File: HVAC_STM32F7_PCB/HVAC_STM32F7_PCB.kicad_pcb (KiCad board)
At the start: 4 copper layers, 200 x 130 mm, 106 parts, among them J1 DC_Jack_5.5x2.1mm, J10 OUT_Signal_connector, J11 OUT_Signal_connector, J12 OUT_Signal_connector, J13 OUT_Signal_connector, J14 Signal_connector, J15 Signal_connector, J16 Signal_connector, J17 Signal_connector, J18 Conn_02x08_Odd_Even, J2 Signal_connector, J3 Signal_connector, J4 Signal_connector, J5 Signal_connector, J6 OUT_Signal_connector, J7 OUT_Signal_connector, J8 OUT_Signal_connector, J9 OUT_Signal_connector, Q1 AO4407A, SW1 ON/OFF, U1 LM2596S-5, U2 LM2596S-3.3, U3 DAC7568IAPW, U5 TLV9304xPW, U6 TLV9304xPW, U7 ADS8688

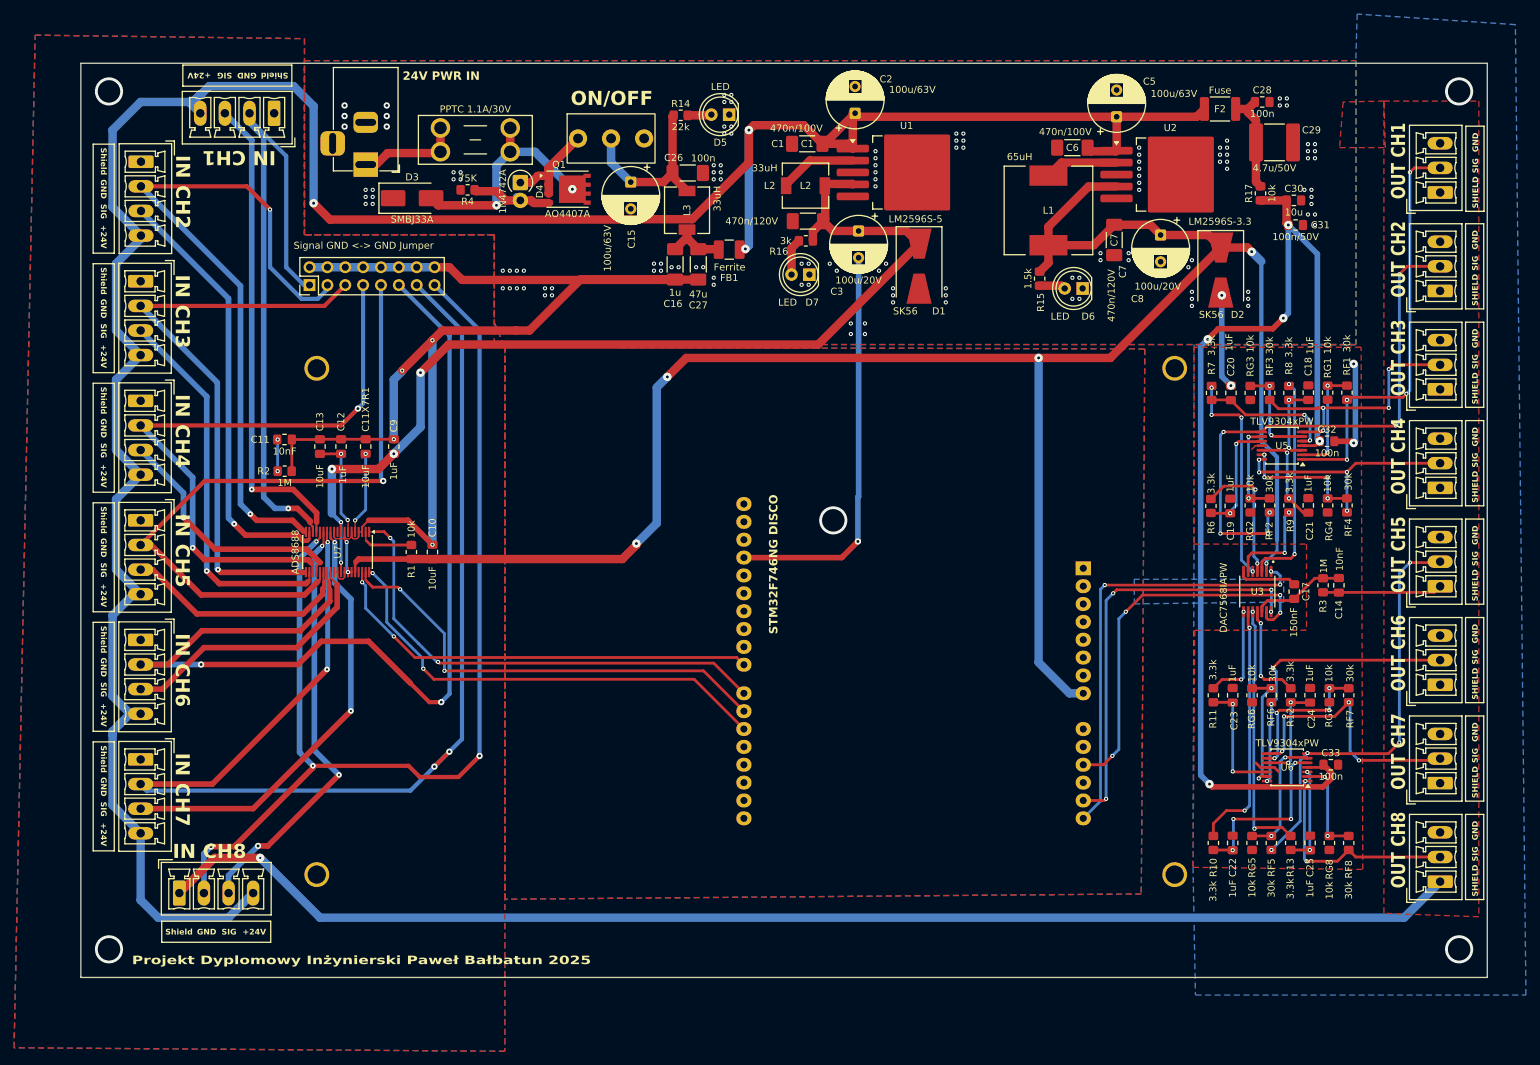
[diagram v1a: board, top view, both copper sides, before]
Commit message: ADD: poprawki pcb, nowe gerbery
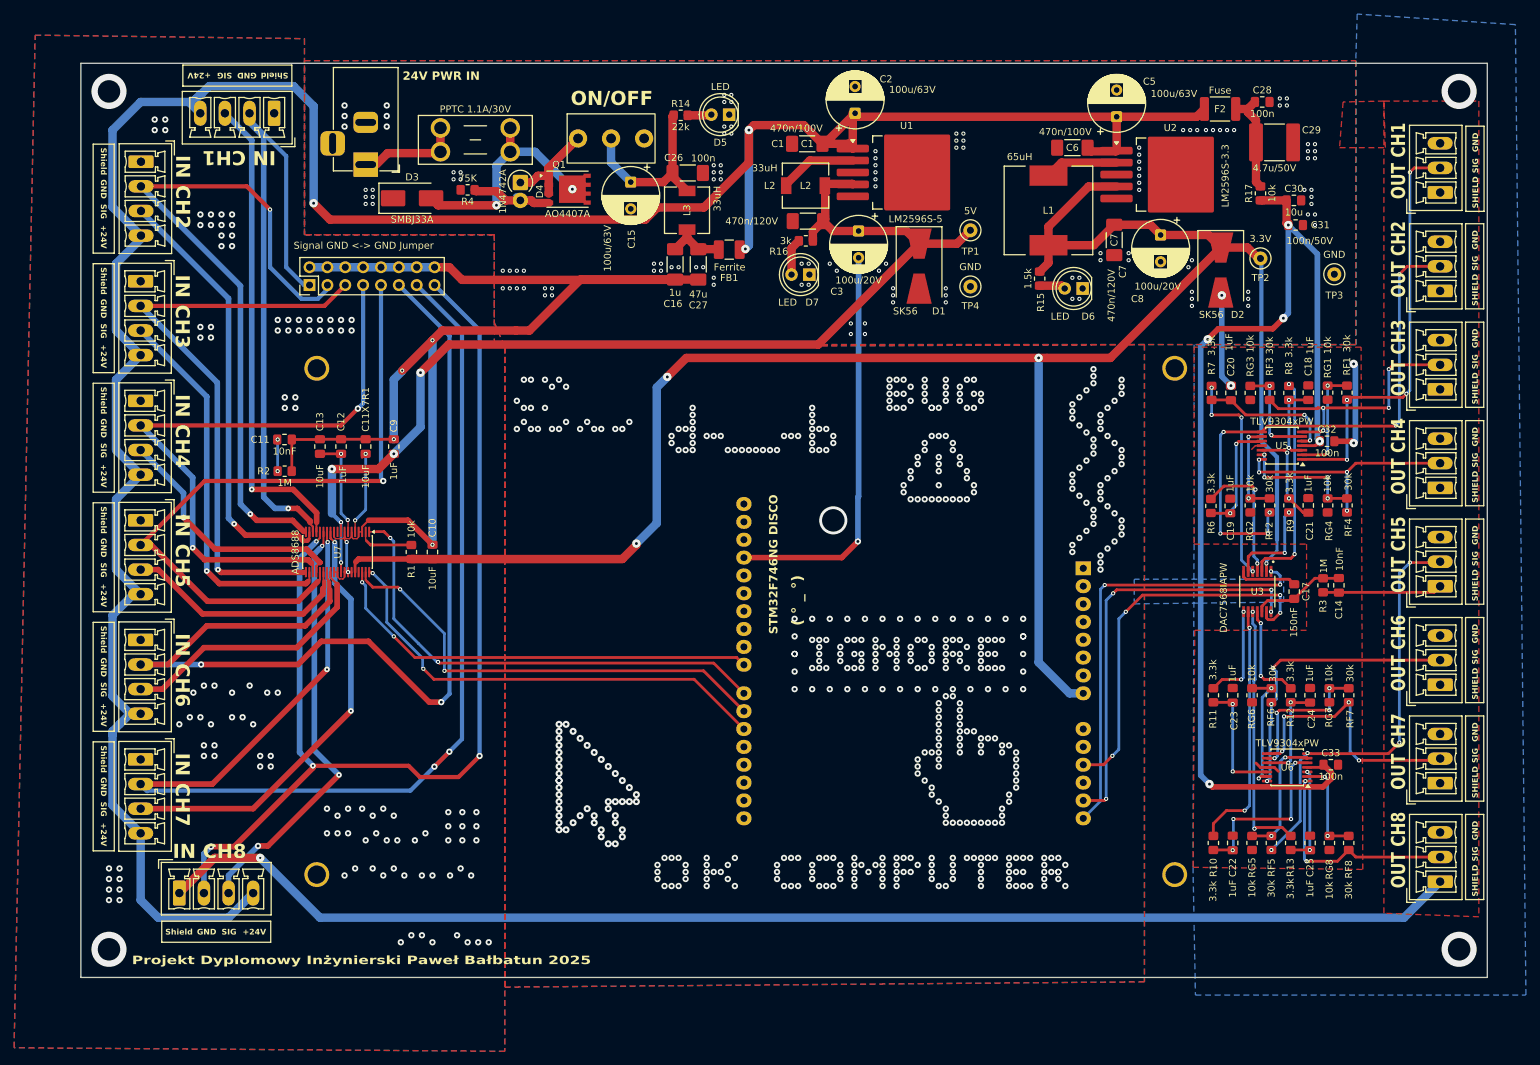
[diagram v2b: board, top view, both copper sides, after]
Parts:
- added TP1: 5V, TestPoint:TestPoint_Loop_D1.80mm_Drill1.0mm_Beaded, F.Cu at (157.5, 54.8)
- added TP2: 3.3V, TestPoint:TestPoint_Loop_D1.80mm_Drill1.0mm_Beaded, F.Cu at (198.8, 58.8)
- added TP3: GND, TestPoint:TestPoint_Loop_D1.80mm_Drill1.0mm_Beaded, F.Cu at (209.2, 61.0)
- added TP4: GND, TestPoint:TestPoint_Loop_D1.80mm_Drill1.0mm_Beaded, F.Cu at (157.5, 62.8)
- renumbered J6 to J21, J7 to J22, J8 to J23, J9 to J24, J10 to J25, J11 to J26, J12 to J27, J13 to J28, J14 to J6, J16 to J7, J17 to J8, J15 to J9
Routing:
- net +5V: track 145.7 -> 153.8 mm
- net Net-(J18-Pin_9): track 96.7 -> 97.4 mm
- net +3.3V: track 304.7 -> 304.1 mm, vias 5 -> 4
- net GNDA: vias 3 -> 117
- net GND: vias 159 -> 669
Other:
- board text added: "( ° _ °)"

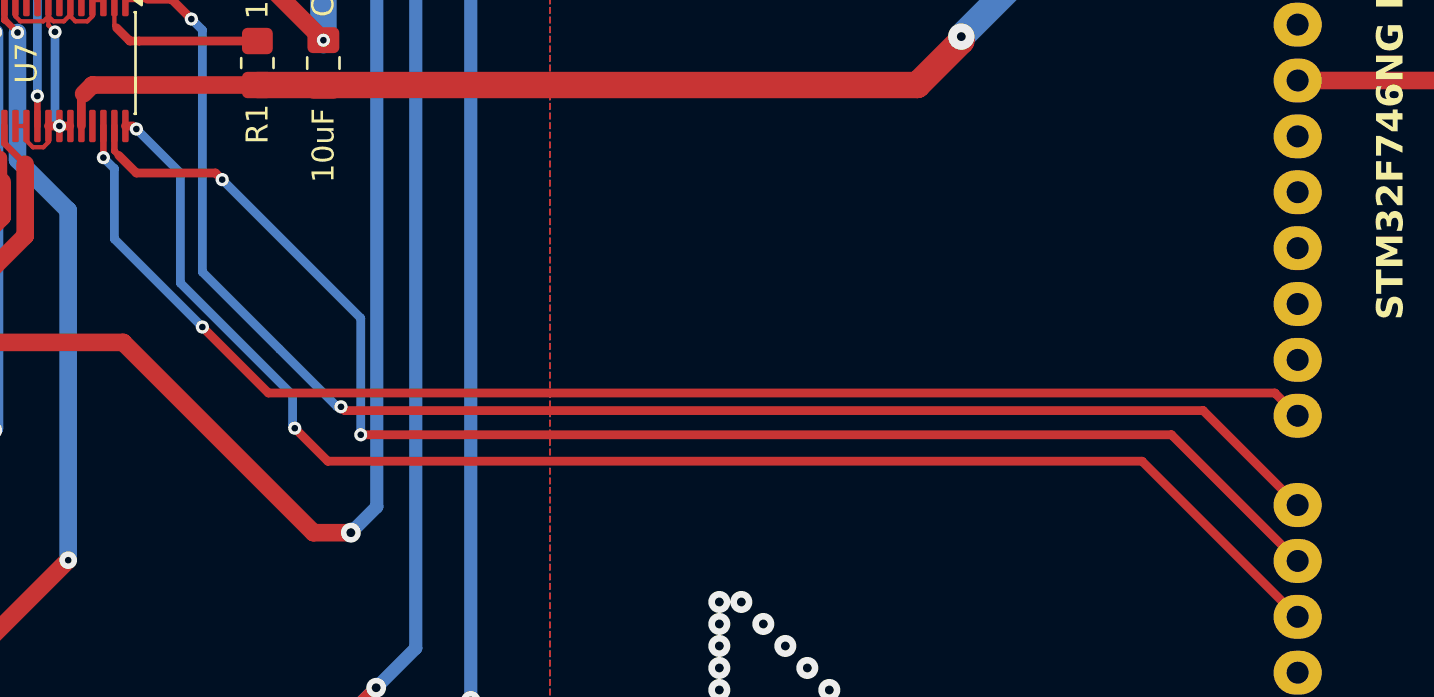
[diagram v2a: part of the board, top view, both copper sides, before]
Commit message: ADD: wgranie ikonek, poprawa parsowania konfiguracji, wizualne zmiany dla bajeranckości, TBA: ekran wglądu sekwencji odzysku ciepła, ikonki dla kanałów I/O
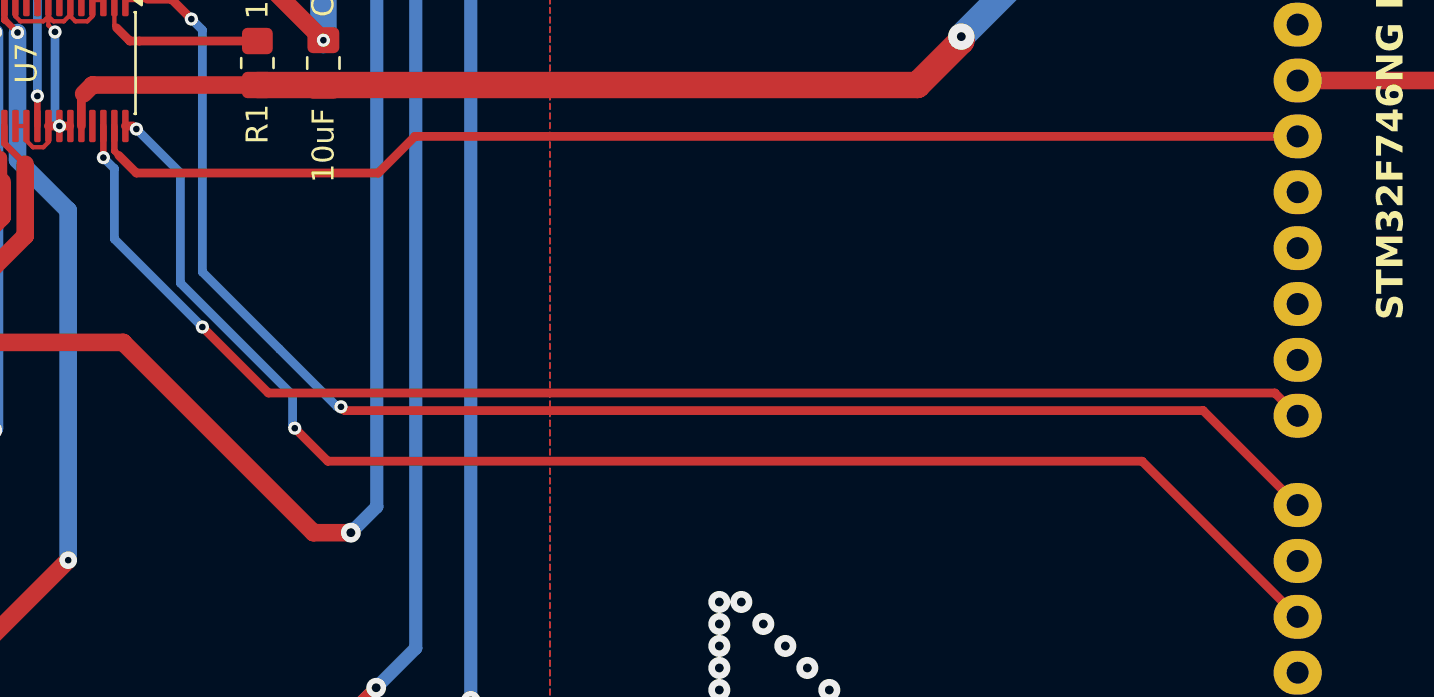
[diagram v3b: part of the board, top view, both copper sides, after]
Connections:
- A1 pad 21: Net-(A1-D6) -> unconnected-(A1-D6-Pad21)
- A1 pad 28: unconnected-(A1-D13-Pad28) -> Net-(A1-D13)
- U7 pad 37: Net-(A1-D6) -> Net-(A1-D13)
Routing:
- net Net-(A1-D6): track 65.8 -> 0.00 mm, vias 2 -> 0
- net Net-(A1-D13): track 0.00 -> 56.0 mm
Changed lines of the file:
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@@
 	(net 60 "Net-(U6A--)")
 	(net 61 "unconnected-(U7-DNC-Pad35)")
-	(net 62 "Net-(A1-D6)")
+	(net 62 "unconnected-(A1-D6-Pad21)")
 	(net 63 "Net-(A1-D8)")
 	(net 64 "Net-(A1-D5)")
@@
 	(net 72 "unconnected-(A1-A3-Pad12)")
 	(net 73 "unconnected-(A1-3V3-Pad4)")
-	(net 74 "unconnected-(A1-D13-Pad28)")
+	(net 74 "Net-(A1-D13)")
 	(net 75 "unconnected-(A1-IOREF-Pad2)")
 	(net 76 "unconnected-(A1-A0-Pad9)")
@@
 			(layers "*.Cu" "*.Mask")
 			(remove_unused_layers no)
-			(net 62 "Net-(A1-D6)")
+			(net 62 "unconnected-(A1-D6-Pad21)")
 			(pinfunction "D6")
-			(pintype "bidirectional")
+			(pintype "bidirectional+no_connect")
 		)
 		(pad "22" thru_hole oval
@@
 			(layers "*.Cu" "*.Mask")
 			(remove_unused_layers no)
-			(net 74 "unconnected-(A1-D13-Pad28)")
+			(net 74 "Net-(A1-D13)")
 			(pinfunction "D13")
-			(pintype "bidirectional+no_connect")
+			(pintype "bidirectional")
 		)
 		(pad "29" thru_hole oval
@@
 			(layers "F.Cu" "F.Mask" "F.Paste")
 			(roundrect_rratio 0.25)
-			(net 62 "Net-(A1-D6)")
+			(net 74 "Net-(A1-D13)")
 			(pinfunction "SCLK")
 			(pintype "input")
@@
 	)
 	(segment
-		(start 82.7 117.4)
-		(end 119.555 117.4)
-		(width 0.4)
-		(layer "F.Cu")
-		(net 62)
-	)
-	(segment
-		(start 119.555 117.4)
-		(end 125.29 123.135)
-		(width 0.4)
-		(layer "F.Cu")
-		(net 62)
-	)
-	(segment
-		(start 71.7 104.7)
-		(end 72.5 105.5)
-		(width 0.4)
-		(layer "F.Cu")
-		(net 62)
-	)
-	(segment
-		(start 72.5 105.5)
-		(end 76.1 105.5)
-		(width 0.4)
-		(layer "F.Cu")
-		(net 62)
-	)
-	(segment
-		(start 71.5 103.3625)
-		(end 71.5 104.5)
-		(width 0.3)
-		(layer "F.Cu")
-		(net 62)
-	)
-	(segment
-		(start 76.1 105.5)
-		(end 76.4 105.8)
-		(width 0.4)
-		(layer "F.Cu")
-		(net 62)
-	)
-	(segment
-		(start 71.5 104.5)
-		(end 71.7 104.7)
-		(width 0.3)
-		(layer "F.Cu")
-		(net 62)
-	)
-	(via
-		(at 82.7 117.4)
-		(size 0.6)
-		(drill 0.3)
-		(layers "F.Cu" "B.Cu")
-		(net 62)
-	)
-	(via
-		(at 76.4 105.8)
-		(size 0.6)
-		(drill 0.3)
-		(layers "F.Cu" "B.Cu")
-		(net 62)
-	)
-	(segment
-		(start 76.4 105.8)
-		(end 82.7 112.1)
-		(width 0.4)
-		(layer "B.Cu")
-		(net 62)
-	)
-	(segment
-		(start 82.7 112.1)
-		(end 82.7 117.4)
-		(width 0.4)
-		(layer "B.Cu")
-		(net 62)
-	)
-	(segment
 		(start 75.5 112.5)
 		(end 78.5 115.5)
@@
 	)
 	(segment
+		(start 71.7 104.7)
+		(end 72.5 105.5)
+		(width 0.4)
+		(layer "F.Cu")
+		(net 74)
+	)
+	(segment
+		(start 72.5 105.5)
+		(end 83.5 105.5)
+		(width 0.4)
+		(layer "F.Cu")
+		(net 74)
+	)
+	(segment
+		(start 83.5 105.5)
+		(end 85.165 103.835)
+		(width 0.4)
+		(layer "F.Cu")
+		(net 74)
+	)
+	(segment
+		(start 85.165 103.835)
+		(end 125.29 103.835)
+		(width 0.4)
+		(layer "F.Cu")
+		(net 74)
+	)
+	(segment
+		(start 71.5 103.3625)
+		(end 71.5 104.5)
+		(width 0.3)
+		(layer "F.Cu")
+		(net 74)
+	)
+	(segment
+		(start 71.5 104.5)
+		(end 71.7 104.7)
+		(width 0.3)
+		(layer "F.Cu")
+		(net 74)
+	)
+	(segment
